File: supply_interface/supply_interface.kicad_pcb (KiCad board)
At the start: 2 copper layers, 93 x 152 mm, 59 parts, among them J1 39-28-1243, J10 MBES-152, J11 MBES-152, J12 MBES-152, J13 MBES-152, J15 3-641215-2, J2 39-28-1043, J3 MBES-152, J4 MBES-152, J5 282837-3, J6 MBES-152, J7 39-28-1043, J8 MBES-152, J9 MBES-152

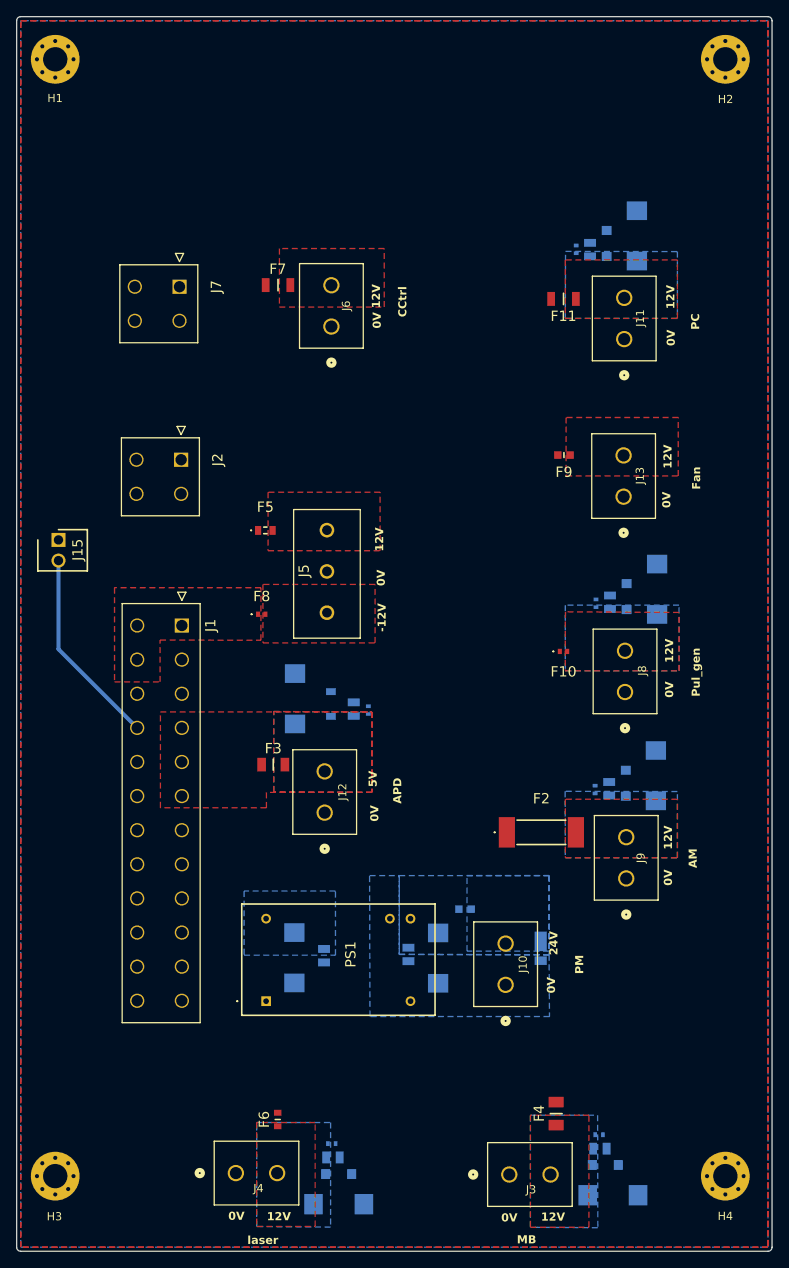
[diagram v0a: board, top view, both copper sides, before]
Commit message: Update supply interface KiCad project and external libraries
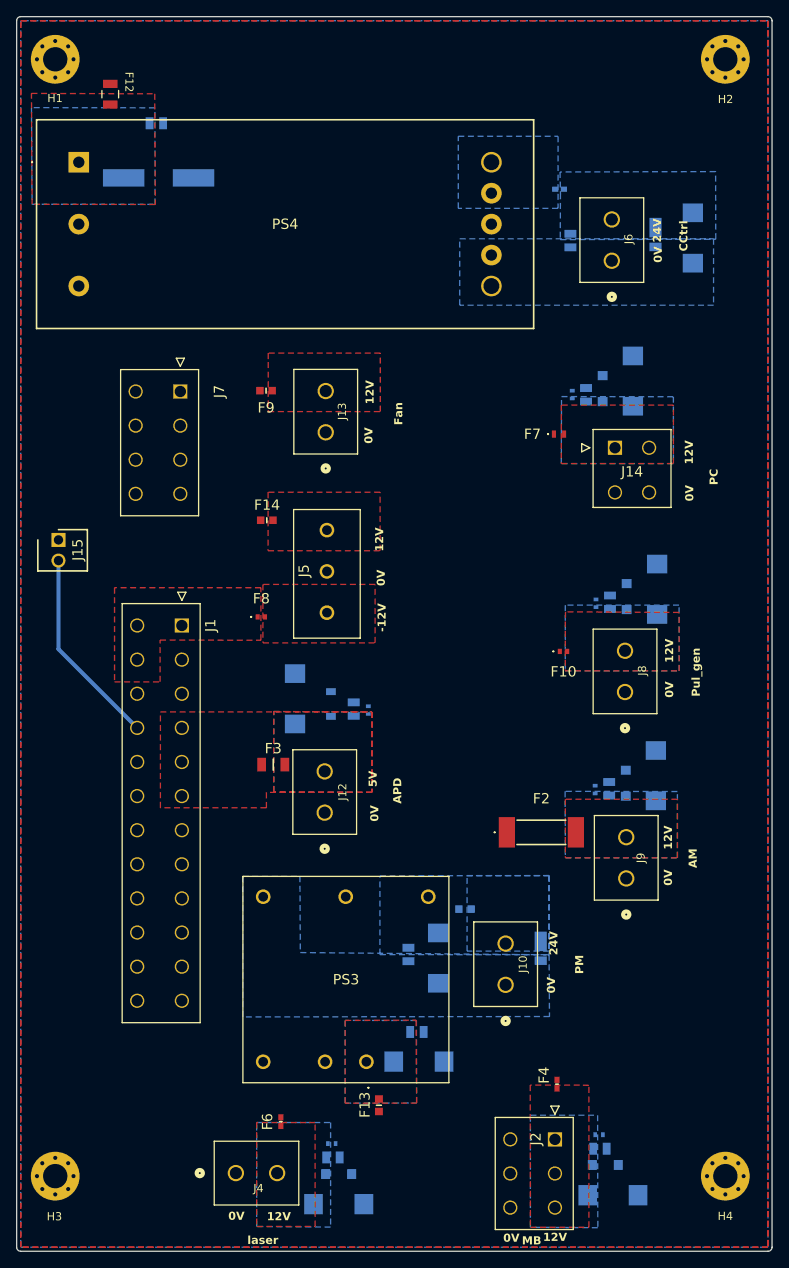
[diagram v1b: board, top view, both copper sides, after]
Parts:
- removed F11: 3413.0329.22, vq:FUSC3216X60N
- removed J11, J3: MBES-152, vq:CONN_MBES-152_ALT
- removed PS1: TEL_15-1215N, vq:TEL151215N
- added C5: 22 uF, vq:CAPC2012X145N, B.Cu at (57.5, 37.9)
- added C6: 220 uF, vq:CAPAE1050X1050N, B.Cu at (57.7, 44.6)
- added C7: 22 uF, vq:CAPC2012X145N, B.Cu at (108.4, 52.3)
- added C8: 100 uF, vq:CAPPM7343X310N, B.Cu at (123.5, 52.0)
- added D8: DFLT27A-7, vq:DFLT27A7, B.Cu at (118.9, 51.6)
- added F12: 20A F.B, vq:FUS_CB_3216FF, F.Cu at (51.8, 34.3)
- added F13: 6A S.B, vq:FUSC1608X95N, F.Cu at (84.8, 158.8)
- added F14: 1.6 S.B, vq:FUSC1608X55N, F.Cu at (71.0, 86.8)
- added J14: 39-28-1043, vq:39-28-1043, F.Cu at (113.9, 77.8)
- added PS3: THN_30-1215, vq:THN302415, F.Cu at (83.3, 153.4)
- added PS4: IRE-24_5-Q12N-C, vq:IRE245Q12NC, F.Cu at (47.9, 42.7)
- C3: value CL21A226MAYNNNE -> 22 uF
- F1: value SF-0603S100-2 -> 0.8 A S.B
- F10, F8: value 0ABA-0200-TN -> 0.2A S.B
- F2: value 3403.0157.24 -> 0.125 A S.B
- F3: value SF-1206S300-2 -> 3A S.B
- F4: value SF-1206S1000R-2 -> 4A S.B; footprint vq:FUSC3216X90N -> vq:FUSC1005X61N
- F5: value 049401.5NRHF -> 4A S.B; footprint vq:0494015NRHF -> vq:FUSC1005X61N; moved to B.Cu
- F6: value 0494002.NRHF -> 4A S.B; footprint vq:FUSC1608X30N -> vq:FUSC1005X61N
- F7: value 3413.0329.22 -> 8A S.B; footprint vq:FUSC3216X60N -> vq:0ABB8000TM
- F9: value SF-0603SP080-2 -> 0.8 A S.B
- J2: value 39-28-1043 -> 39-28-1063; footprint vq:39-28-1043 -> vq:39-28-1063
- J7: value 39-28-1043 -> 39-28-1083; footprint vq:39-28-1043 -> vq:39-28-1083
- moved J2 95.5 mm to (106.5, 163.0)
- moved F5 55.5 mm to (107.1, 46.0), turned to 180 degrees
- moved F7 39.2 mm to (107.0, 76.2)
- moved F9 37.5 mm to (71.0, 70.8)
- moved J13 37.5 mm to (78.3, 75.9)
- moved J6 35.5 mm to (113.5, 54.8)
- moved C1 20.0 mm to (89.8, 153.4), turned to 0 degrees
- moved C21 17.9 mm to (108.7, 71.3)
- moved C22 17.9 mm to (110.3, 71.3)
- moved C23 17.9 mm to (116.1, 69.6)
- moved D5 17.9 mm to (112.4, 70.5)
- moved C3 14.8 mm to (89.5, 149.8), turned to 180 degrees
- moved J7 12.9 mm to (60.4, 70.9)
- moved F4 3.63 mm to (106.8, 156.2)
- moved F6 0.47 mm to (72.8, 160.8)
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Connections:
- C1 pad 1: 12V -> Net-(PS3-+VIN_(VCC))
- C3 pad 2: 12V -> Net-(PS3-+VIN_(VCC))
- F5 pad 1: 12V -> /cctrl
- F5 pad 2: /pol_p -> /SENS_P
- F7 pad 2: /peltier -> /pc
- J2 pad 1: 12V -> /MB
- J2 pad 2: 12V -> /MB
- J2 pad 3: GND -> /MB
- J6 pad 1: GND -> /GND_cctrl
- J6 pad 2: /peltier -> /cctrl
- J7 pad 3: GND -> 12V
- J7 pad 4: GND -> 12V
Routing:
- added copper zone on B.Cu, net /GND_cctrl
- added copper zone on B.Cu, net /SENS_P
- added copper zone on B.Cu, net /cctrl
- added copper zone on B.Cu, net /vin+_120w
- added copper zone on F.Cu, net /vin+_120w
- added copper zone on B.Cu, net Net-(PS3-+VIN_(VCC))
- added copper zone on F.Cu, net Net-(PS3-+VIN_(VCC))
- removed copper zone on F.Cu, net /peltier
- removed copper zone on B.Cu, net 12V

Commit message: update computer fuse
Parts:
- F7: value 8A S.B -> SF-1206S1000R-2; footprint vq:0ABB8000TM -> vq:FUSC3216X90N
- moved F7 1.15 mm to (107.1, 75.0)
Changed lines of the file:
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@@
       (net 18 "/laser") (pinfunction "2") (pintype "unspecified"))
+  )
+  (footprint "vq:FUSC3216X90N" (layer "F.Cu")
+    (at 107.1 75)
+    (descr "SF-1206S1000R-2")
+    (tags "Fuse")
+    (property "Height" "0.9")
+    (property "Manufacturer_Name" "Bourns")
+    (property "Manufacturer_Part_Number" "SF-1206S1000R-2")
+    (property "Mouser Part Number" "652-SF-1206S1000R-2")
+    (property "Mouser Price/Stock" "https://www.mouser.co.uk/ProductDetail/Bourns/SF-1206S1000R-2?qs=QpmGXVUTftGXxpZRDDQNPQ%3D%3D")
+    (property "Sheetfile" "supply_interface.kicad_sch")
+    (property "Sheetname" "")
+    (property "ki_description" "1206 slow-blow met-foil. 10A")
+    (attr smd)
+    (fp_text reference "F7" (at -4.2 -0.025) (layer "F.SilkS")
+        (effects (font (size 1.27 1.27) (thickness 0.254)))
+    )
+    (fp_text value "SF-1206S1000R-2" (at 0 0) (layer "F.SilkS") hide
+        (effects (font (size 1.27 1.27) (thickness 0.254)))
+    )
+    (fp_text user "${REFERENCE}" (at -4.2 -0.025) (layer "F.Fab")
+        (effects (font (size 1.27 1.27) (thickness 0.254)))
+    )
+    (fp_line (start 0 -0.725) (end 0 0.725)
+      (stroke (width 0.2) (type solid)) (layer "F.SilkS"))
+    (fp_line (start -2.31 -1.185) (end 2.31 -1.185)
+      (stroke (width 0.05) (type solid)) (layer "F.CrtYd"))
+    (fp_line (start -2.31 1.185) (end -2.31 -1.185)
+      (stroke (width 0.05) (type solid)) (layer "F.CrtYd"))
+    (fp_line (start 2.31 -1.185) (end 2.31 1.185)
+      (stroke (width 0.05) (type solid)) (layer "F.CrtYd"))
+    (fp_line (start 2.31 1.185) (end -2.31 1.185)
+      (stroke (width 0.05) (type solid)) (layer "F.CrtYd"))
+    (fp_line (start -1.6 -0.825) (end 1.6 -0.825)
+      (stroke (width 0.1) (type solid)) (layer "F.Fab"))
+    (fp_line (start -1.6 0.825) (end -1.6 -0.825)
+      (stroke (width 0.1) (type solid)) (layer "F.Fab"))
+    (fp_line (start 1.6 -0.825) (end 1.6 0.825)
+      (stroke (width 0.1) (type solid)) (layer "F.Fab"))
+    (fp_line (start 1.6 0.825) (end -1.6 0.825)
+      (stroke (width 0.1) (type solid)) (layer "F.Fab"))
+    (pad "1" smd rect (at -1.415 0) (size 1.29 1.87) (layers "F.Cu" "F.Paste" "F.Mask")
+      (net 6 "12V") (pinfunction "1") (pintype "passive"))
+    (pad "2" smd rect (at 1.415 0) (size 1.29 1.87) (layers "F.Cu" "F.Paste" "F.Mask")
+      (net 16 "/pc") (pinfunction "2") (pintype "passive"))
+    (model "SF-1206S1000R-2.stp"
+      (offset (xyz 0 0 0))
+      (scale (xyz 1 1 1))
+      (rotate (xyz 0 0 0))
+    )
   )
   (footprint "vq:FUSC1608X95N" (layer "F.Cu")
@@
     )
   )
-  (footprint "vq:0ABB8000TM" (layer "F.Cu")
-    (at 107.025 76.15)
-    (descr "0ABB-8000-TM-1")
-    (tags "Fuse")
-    (property "Height" "0.56")
-    (property "Manufacturer_Name" "BelFuse")
-    (property "Manufacturer_Part_Number" "0ABB-8000-TM")
-    (property "Mouser Part Number" "530-0ABB-8000-TM")
-    (property "Mouser Price/Stock" "https://www.mouser.co.uk/ProductDetail/Bel-Fuse/0ABB-8000-TM?qs=Wj%2FVkw3K%252BMB%2Fdij68u0w3Q%3D%3D")
-    (property "Sheetfile" "supply_interface.kicad_sch")
-    (property "Sheetname" "")
-    (property "ki_description" "Fuse Chip 8A 32V SMD Solder Pad 0603 Ceramic Automotive")
-    (attr smd)
-    (fp_text reference "F7" (at -3.275 0) (layer "F.SilkS")
-        (effects (font (size 1.27 1.27) (thickness 0.254)))
-    )
-    (fp_text value "8A S.B" (at 0 0) (layer "F.SilkS") hide
-        (effects (font (size 1.27 1.27) (thickness 0.254)))
-    )
-    (fp_text user "${REFERENCE}" (at -3.275 0) (layer "F.Fab")
-        (effects (font (size 1.27 1.27) (thickness 0.254)))
-    )
-    (fp_line (start -1.4 0) (end -1.4 0)
-      (stroke (width 0.1) (type solid)) (layer "F.SilkS"))
-    (fp_line (start -1.3 0) (end -1.3 0)
-      (stroke (width 0.1) (type solid)) (layer "F.SilkS"))
-    (fp_arc (start -1.4 0) (mid -1.35 -0.05) (end -1.3 0)
-      (stroke (width 0.1) (type solid)) (layer "F.SilkS"))
-    (fp_arc (start -1.3 0) (mid -1.35 0.05) (end -1.4 0)
-      (stroke (width 0.1) (type solid)) (layer "F.SilkS"))
-    (fp_line (start -1.875 -1.45) (end 1.875 -1.45)
-      (stroke (width 0.1) (type solid)) (layer "F.CrtYd"))
-    (fp_line (start -1.875 1.45) (end -1.875 -1.45)
-      (stroke (width 0.1) (type solid)) (layer "F.CrtYd"))
-    (fp_line (start 1.875 -1.45) (end 1.875 1.45)
-      (stroke (width 0.1) (type solid)) (layer "F.CrtYd"))
-    (fp_line (start 1.875 1.45) (end -1.875 1.45)
-      (stroke (width 0.1) (type solid)) (layer "F.CrtYd"))
-    (fp_line (start -0.8 -0.405) (end 0.8 -0.405)
-      (stroke (width 0.1) (type solid)) (layer "F.Fab"))
-    (fp_line (start -0.8 0.405) (end -0.8 -0.405)
-      (stroke (width 0.1) (type solid)) (layer "F.Fab"))
-    (fp_line (start 0.8 -0.405) (end 0.8 0.405)
-      (stroke (width 0.1) (type solid)) (layer "F.Fab"))
-    (fp_line (start 0.8 0.405) (end -0.8 0.405)
-      (stroke (width 0.1) (type solid)) (layer "F.Fab"))
-    (pad "1" smd rect (at -0.625 0) (size 0.5 0.9) (layers "F.Cu" "F.Paste" "F.Mask")
-      (net 6 "12V") (pinfunction "1") (pintype "passive"))
-    (pad "2" smd rect (at 0.625 0) (size 0.5 0.9) (layers "F.Cu" "F.Paste" "F.Mask")
-      (net 16 "/pc") (pinfunction "2") (pintype "passive"))
-  )
   (footprint "vq:39-28-1083" (layer "F.Cu")
